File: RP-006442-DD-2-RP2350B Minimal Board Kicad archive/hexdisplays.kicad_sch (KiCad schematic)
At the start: 3 parts, among them U8 HT16K33A-24SSOP, U9 CC56-12EWA

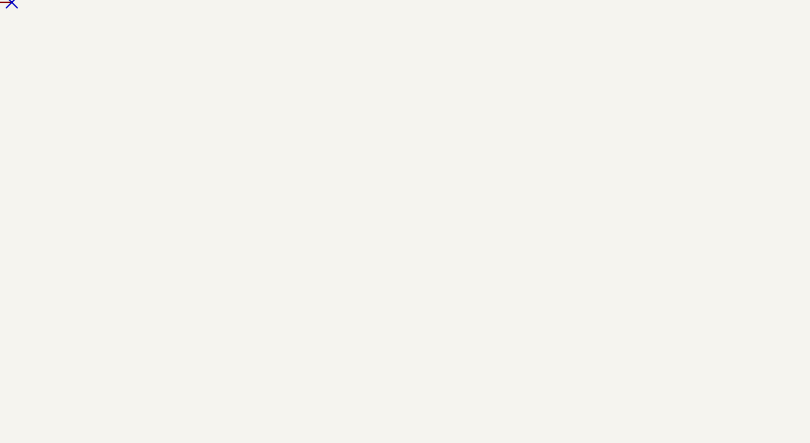
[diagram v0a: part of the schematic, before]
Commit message: Added GS3011CR-G symbol and footprint
GS3011CR-G SMD 7-segment display from jlcpcb
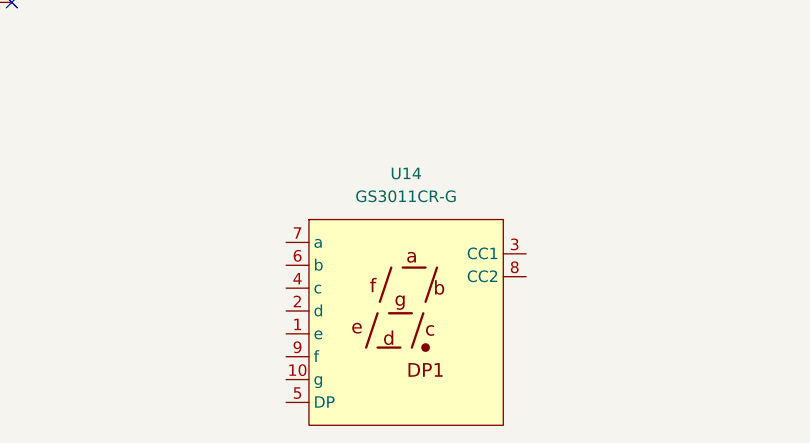
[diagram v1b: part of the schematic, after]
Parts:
- added U14: GS3011CR-G, custom:GS3011CR-G, symbol GS3011CR-G:GS3011CR-G
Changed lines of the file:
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@@
+	)
+	(symbol
+		(lib_id "GS3011CR-G:GS3011CR-G")
+		(at 127 146.05 0)
+		(unit 1)
+		(exclude_from_sim no)
+		(in_bom yes)
+		(on_board yes)
+		(dnp no)
+		(fields_autoplaced yes)
+		(property "Reference" "U14"
+			(at 137.795 140.97 0)
+			(effects
+				(font
+					(size 1.27 1.27)
+				)
+			)
+		)
+		(property "Value" "GS3011CR-G"
+			(at 137.795 143.51 0)
+			(effects
+				(font
+					(size 1.27 1.27)
+				)
+			)
+		)
+		(property "Footprint" "custom:GS3011CR-G"
+			(at 127 146.05 0)
+			(effects
+				(font
+					(size 1.27 1.27)
+				)
+				(hide yes)
+			)
+		)
+		(property "Datasheet" "https://jlcpcb.com/api/file/downloadByFileSystemAccessId/8603393381133398016"
+			(at 127 146.05 0)
+			(effects
+				(font
+					(size 1.27 1.27)
+				)
+				(hide yes)
+			)
+		)
+		(property "Description" ""
+			(at 127 146.05 0)
+			(effects
+				(font
+					(size 1.27 1.27)
+				)
+				(hide yes)
+			)
+		)
+		(pin "2"
+		)
+		(pin "7"
+		)
+		(pin "1"
+		)
+		(pin "9"
+		)
+		(pin "3"
+		)
+		(pin "6"
+		)
+		(pin "8"
+		)
+		(pin "10"
+		)
+		(pin "4"
+		)
+		(pin "5"
+		)
+		(instances
+			(project ""
+				(path "/94683f5c-9cd9-448e-be96-9792537b5cb8/09473c75-4602-45fc-a2db-44d591bf96bf"
+					(reference "U14")
+					(unit 1)
+				)
+			)
+		)
 	)
 	(symbol

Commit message: Testing electrical rules
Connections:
- net COM0: now also U14.3 (CC1)
- net COM1: now also U14.8 (CC2)
- net ROW0: now also U14.7 (a)
- net ROW1: now also U14.6 (b)
- net ROW2: now also U14.4 (c)
- net ROW3: now also U14.2 (d)
- net ROW4: now also U14.1 (e)
- net ROW5: now also U14.9 (f)
- net ROW6: now also U14.10 (g)
- net ROW7: now also U14.5 (DP)
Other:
- moved on the sheet: U14

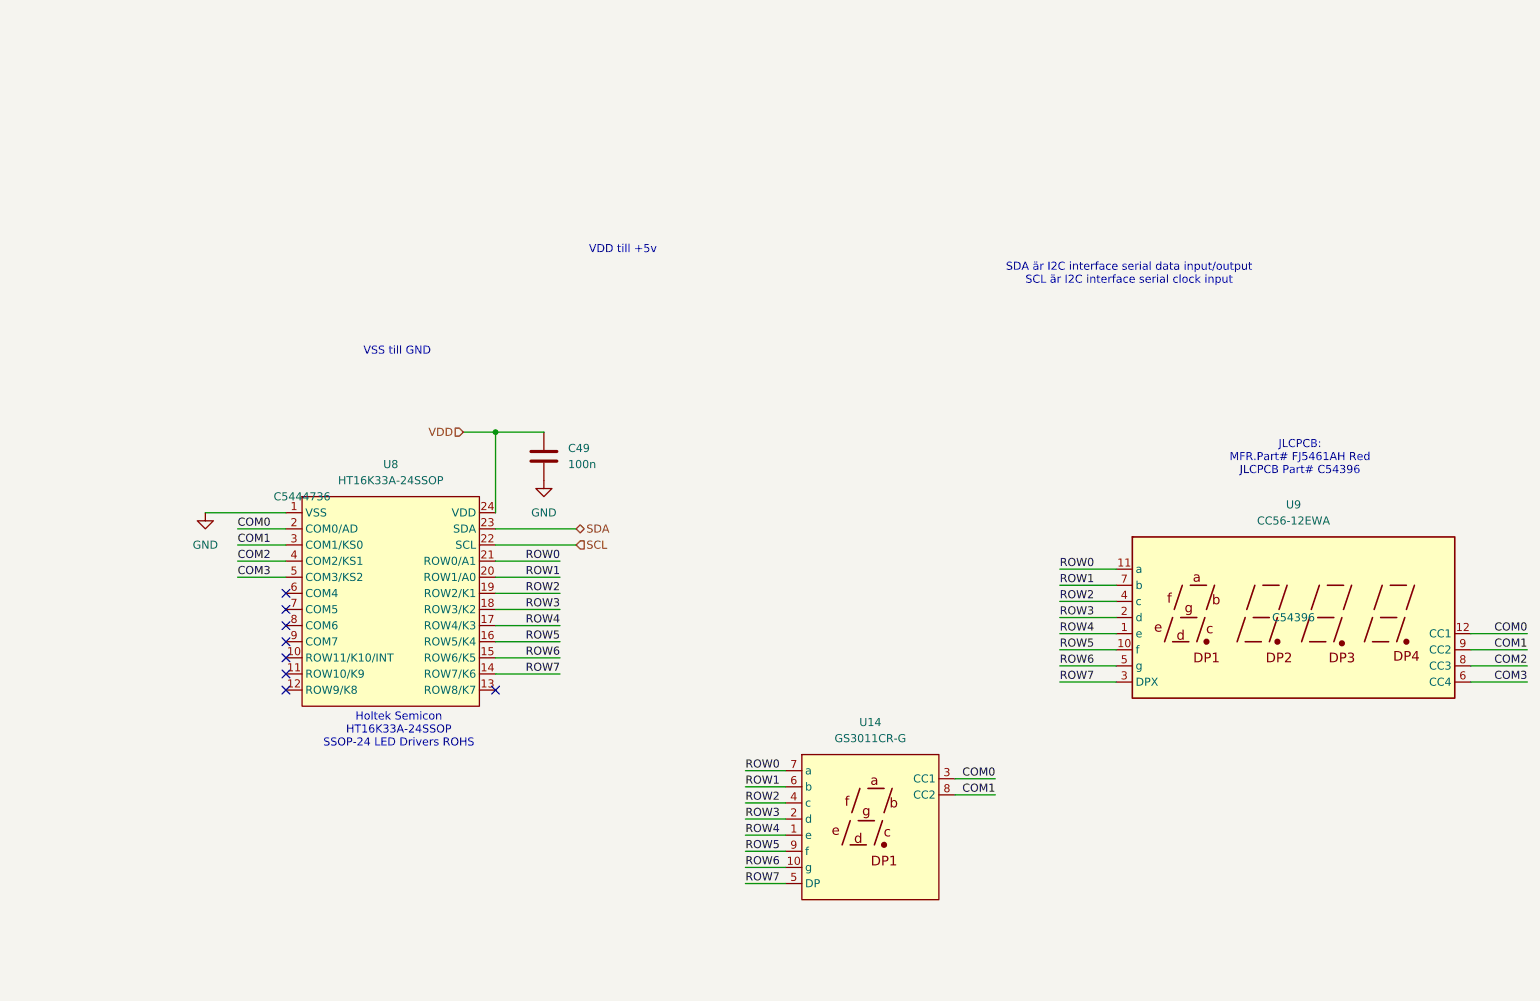
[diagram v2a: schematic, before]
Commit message: Update GS3011CR-G footprint
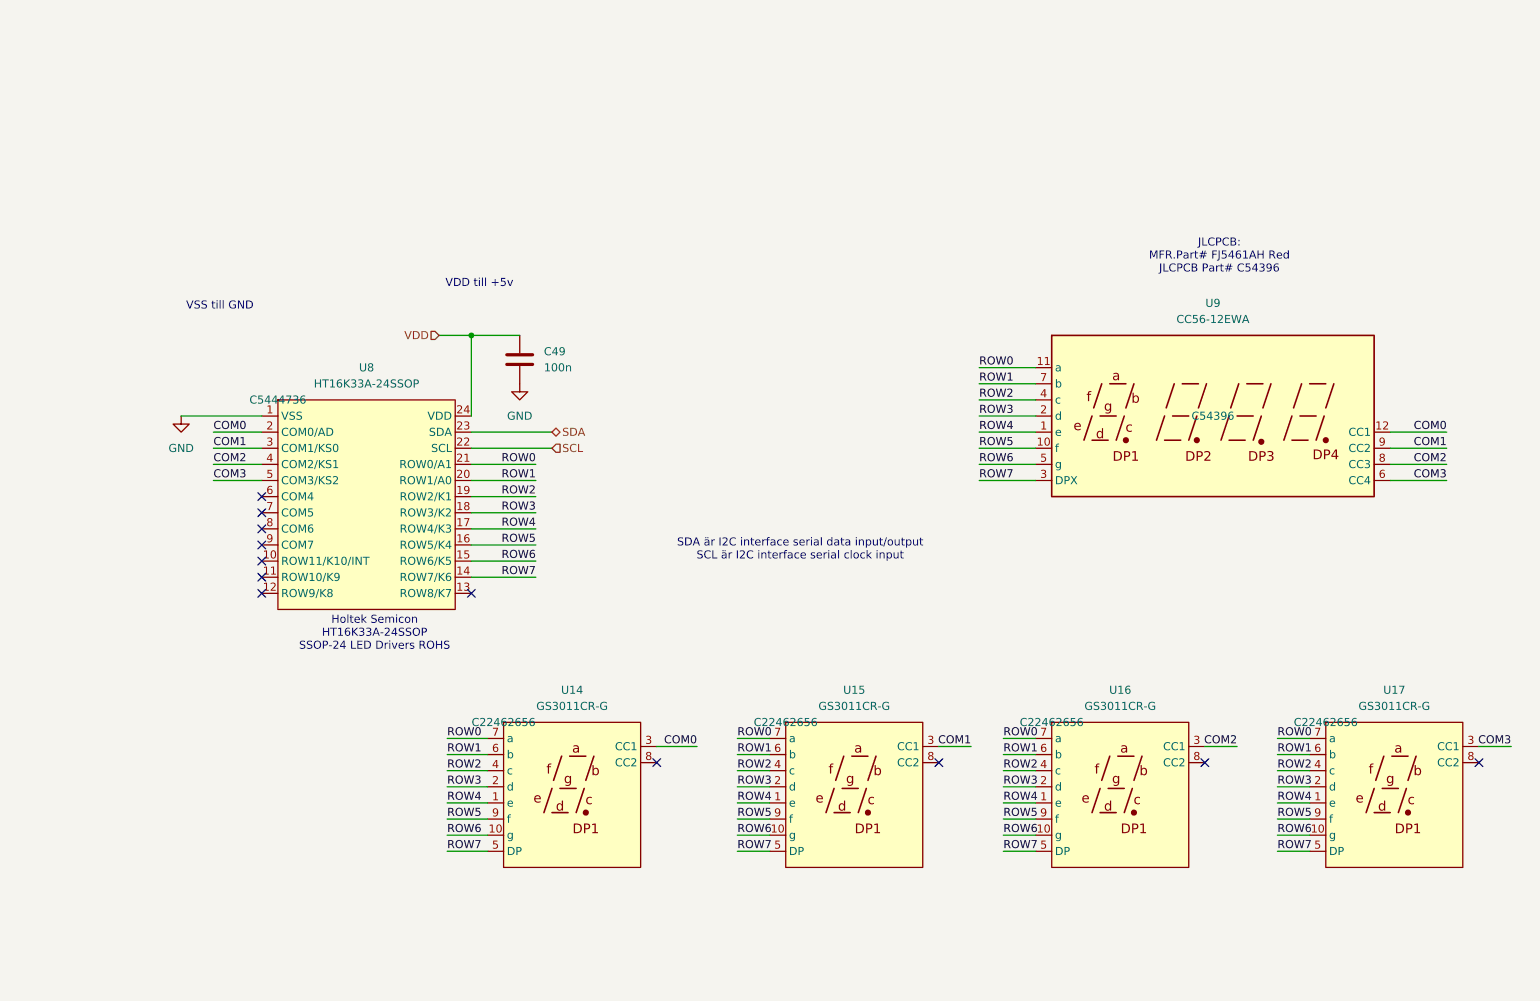
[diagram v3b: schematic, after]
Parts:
- added U15, U16, U17: GS3011CR-G, GS3011CR-G:GS3011CR-G, symbol GS3011CR-G:GS3011CR-G
- U14: footprint custom:GS3011CR-G -> GS3011CR-G:GS3011CR-G; LCSC (none) -> C22462656
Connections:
- net COM1: now also U15.3 (CC1); no longer U14.8 (CC2)
- net COM2: now also U16.3 (CC1)
- net COM3: now also U17.3 (CC1)
- net ROW0: now also U15.7 (a), U16.7 (a), U17.7 (a)
- net ROW1: now also U15.6 (b), U16.6 (b), U17.6 (b)
- net ROW2: now also U15.4 (c), U16.4 (c), U17.4 (c)
- net ROW3: now also U15.2 (d), U16.2 (d), U17.2 (d)
- net ROW4: now also U15.1 (e), U16.1 (e), U17.1 (e)
- net ROW5: now also U15.9 (f), U16.9 (f), U17.9 (f)
- net ROW6: now also U15.10 (g), U16.10 (g), U17.10 (g)
- net ROW7: now also U15.5 (DP), U16.5 (DP), U17.5 (DP)
- no-connect marks 8 -> 12
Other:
- moved on the sheet: C49, U14, U8, U9

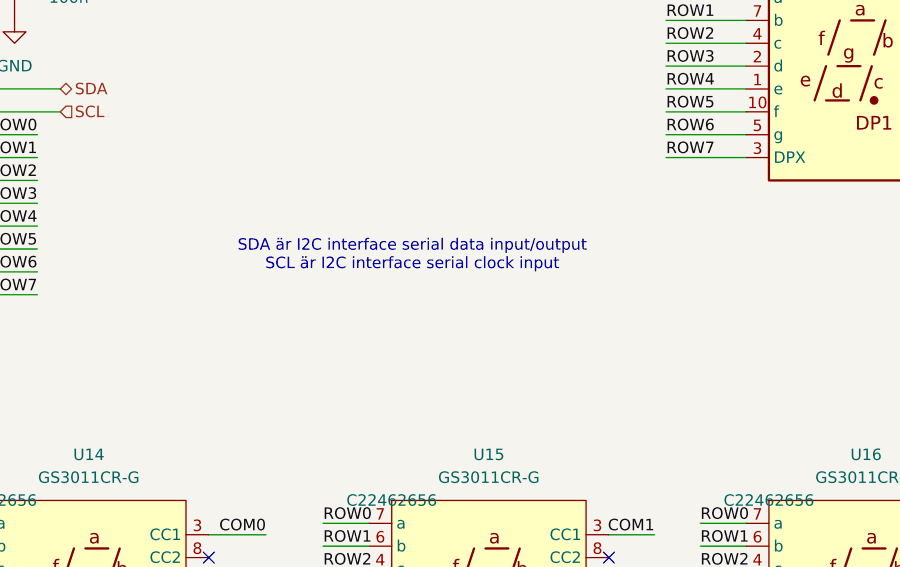
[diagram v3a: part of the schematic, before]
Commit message: Update hex display pcb traces
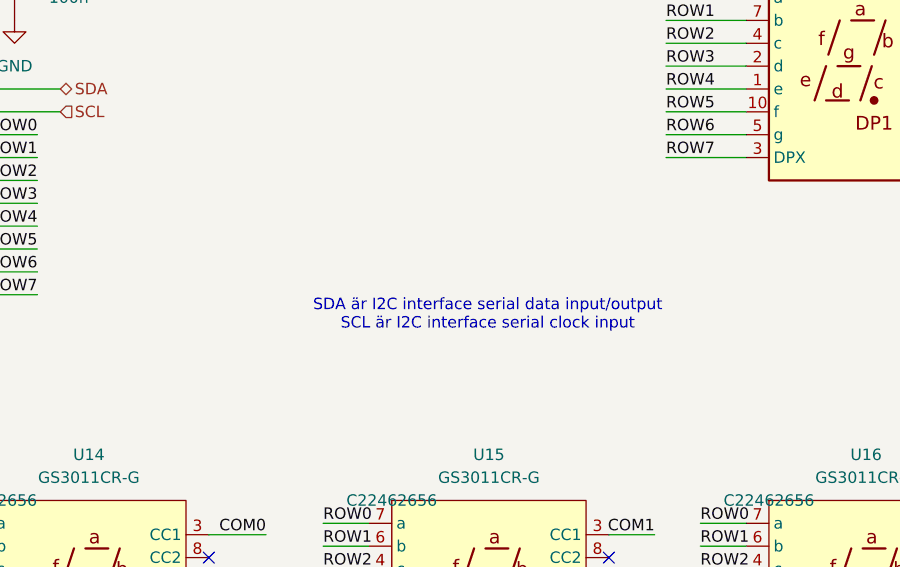
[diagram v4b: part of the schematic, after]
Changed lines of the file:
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@@
 	(text "SDA är I2C interface serial data input/output\nSCL är I2C interface serial clock input"
 		(exclude_from_sim no)
-		(at 141.986 99.822 0)
+		(at 150.368 106.426 0)
 		(effects
 			(font

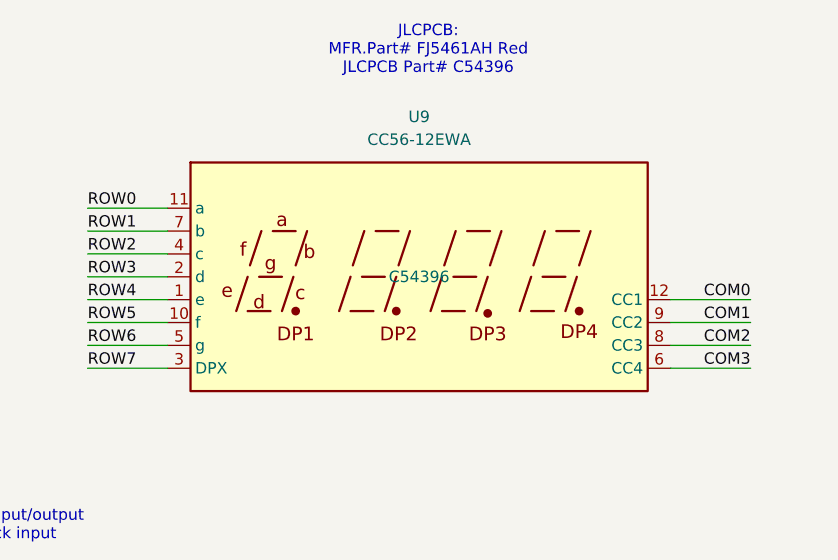
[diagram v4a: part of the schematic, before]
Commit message: Update usb power switch
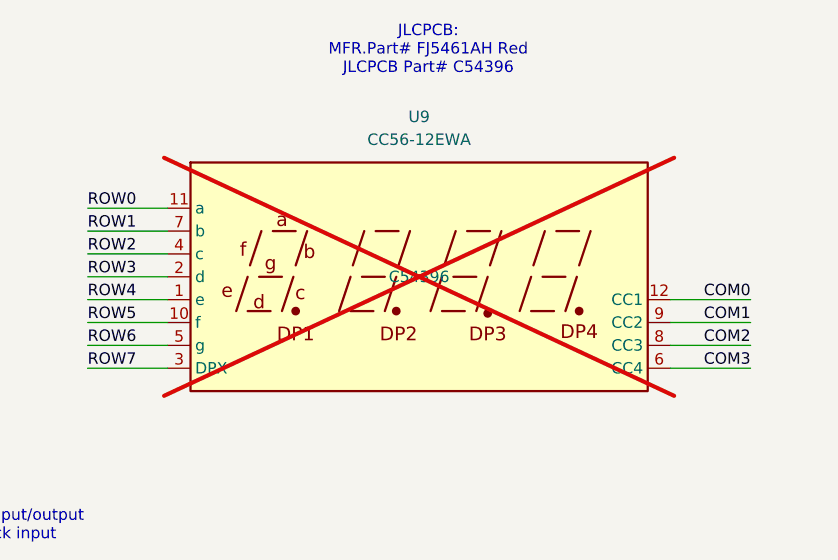
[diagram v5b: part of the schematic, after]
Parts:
- U9: now not fitted
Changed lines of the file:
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@@
 		(in_bom yes)
 		(on_board yes)
-		(dnp no)
+		(dnp yes)
 		(fields_autoplaced yes)
 		(property "Reference" "U9"

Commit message: Production files
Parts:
- removed U9: CC56-12EWA, Display_7Segment:CA56-12EWA, symbol Display_Character:CC56-12EWA
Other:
- note removed: "JLCPCB: MFR.Part# FJ5461AH Red JLCPCB Part# C54396"

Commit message: Created Figures
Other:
- note added: "SDA, I2C interface serial data input/output SCL, I2C interface serial clock input"
- note removed: "SDA är I2C interface serial data input/output SCL är I2C interface serial clock input"
- note removed: "VDD till +5v"
- note removed: "VSS till GND"
- moved on the sheet: C49, U14, U15, U16, U17, U8
